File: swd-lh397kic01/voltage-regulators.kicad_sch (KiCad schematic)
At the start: 10 parts, among them U1 RS3236-2.5FY5, U3 AP3127B

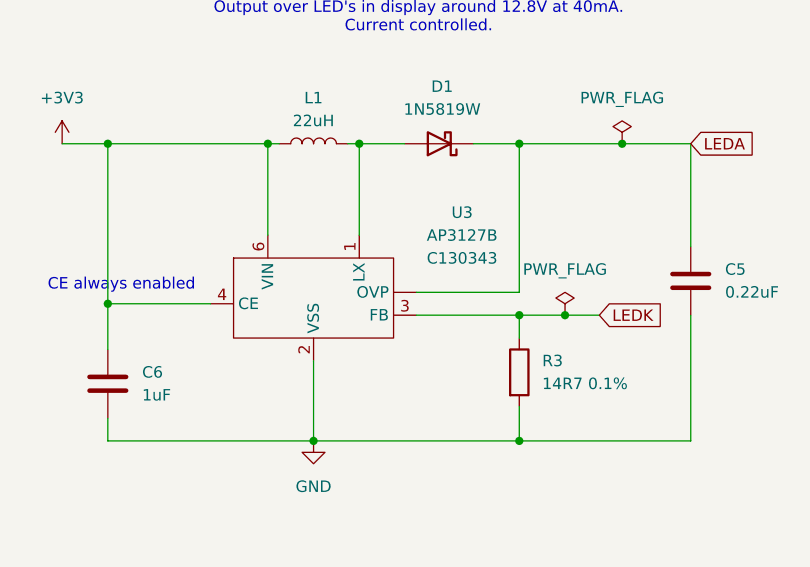
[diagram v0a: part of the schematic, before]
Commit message: Fix names, footprints, and silkscreen of the pcb's
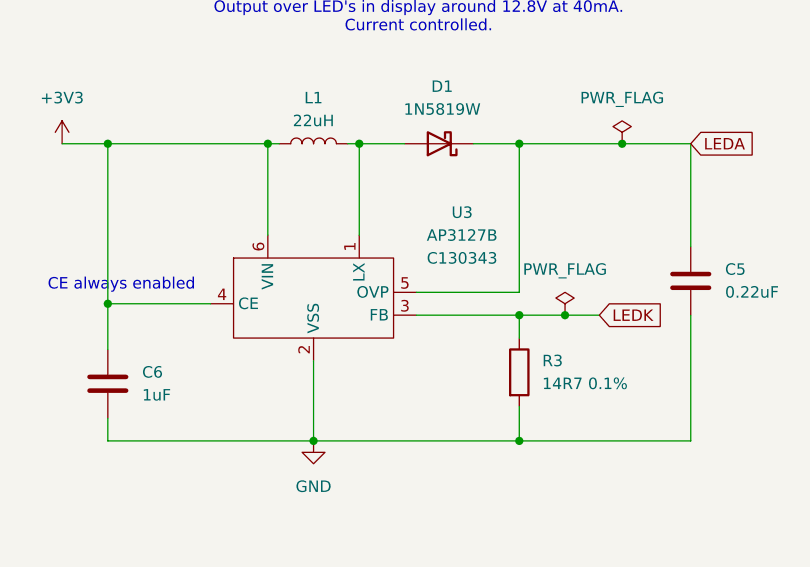
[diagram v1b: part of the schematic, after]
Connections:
- net LEDA: now also U3.5 (OVP); no longer U3. (OVP)
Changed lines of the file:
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@@
 		(pin "1"
 		)
-		(pin ""
+		(pin "5"
 		)
 		(pin "2"

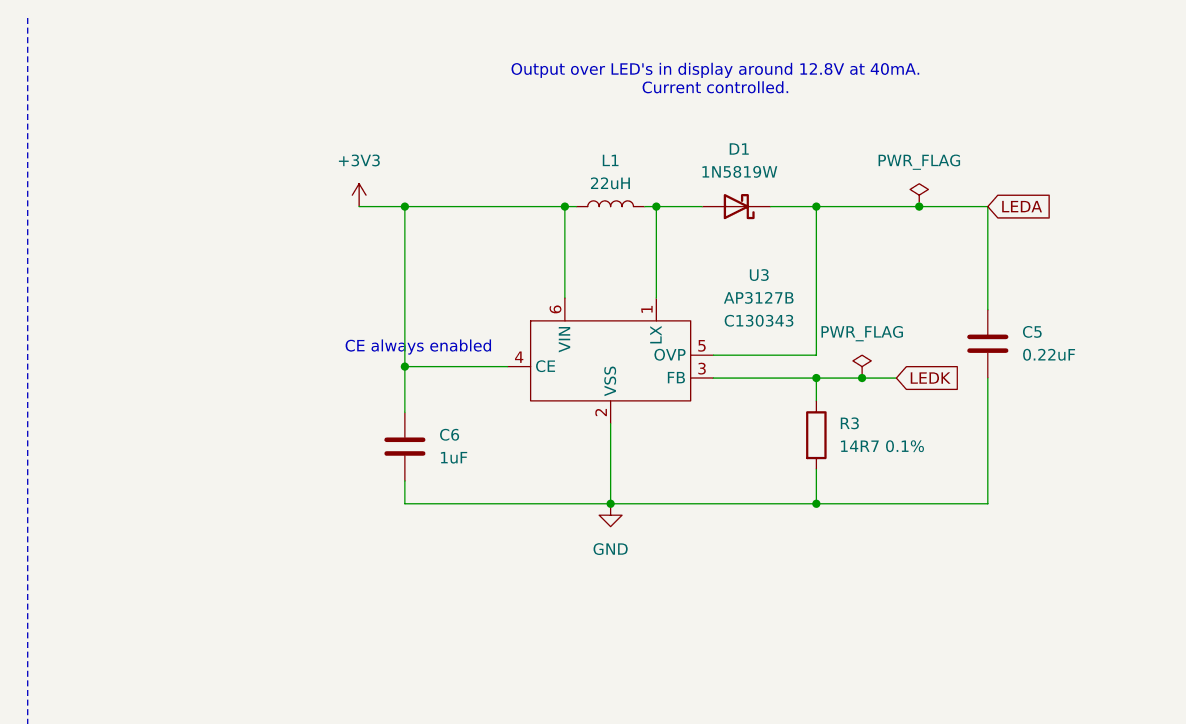
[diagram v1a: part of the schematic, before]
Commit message: Add LCSC labels that were missing for swd lh397kic01
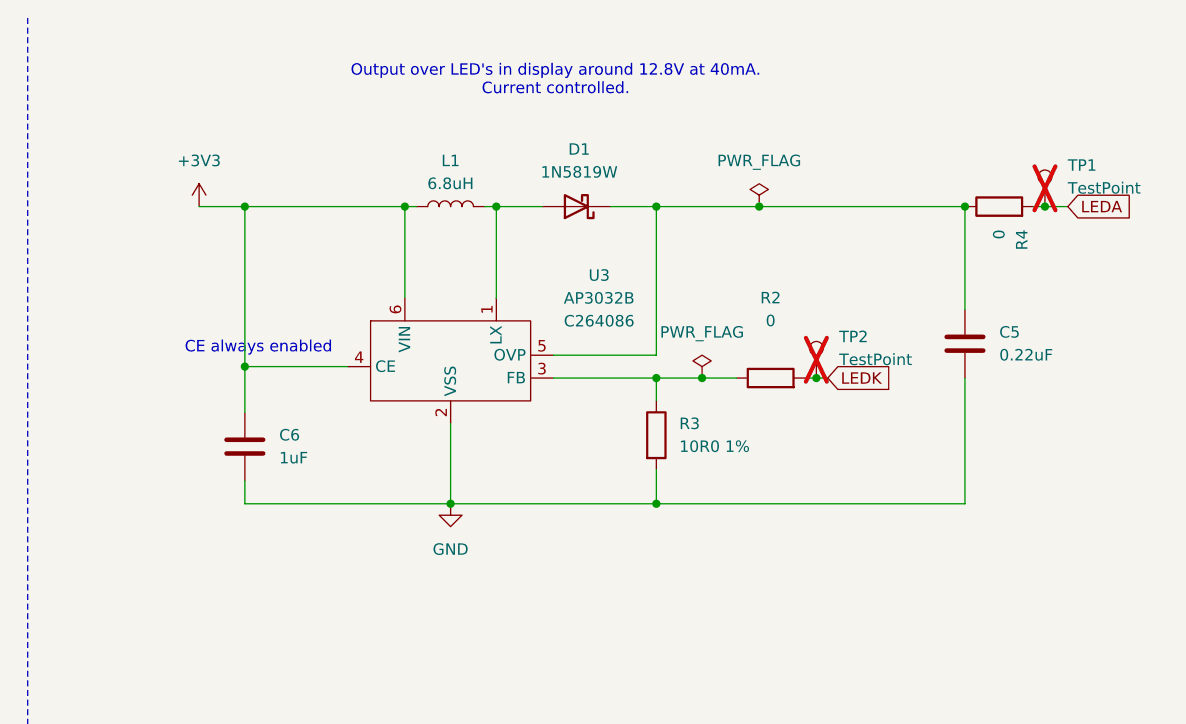
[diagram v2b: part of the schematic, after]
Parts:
- added R2, R4: 0, Resistor_SMD:R_0603_1608Metric, symbol Device:R
- added TP1, TP2: TestPoint, TestPoint:TestPoint_Pad_D1.0mm, symbol Connector:TestPoint
- C1, C2, C3, C6: LCSC C5189821 -> C386149
- L1: value 22uH -> 6.8uH; footprint Inductor_SMD:L_Changjiang_FNR252010S -> Inductor_SMD:L_1210_3225Metric_Pad1.42x2.65mm_HandSolder; LCSC C486445 -> C394999
- R3: value 14R7 0.1% -> 10R0 1%; LCSC C861135 -> C103222
- U1: LCSC (none) -> C379345; Lcsc C379345 -> (none)
- U3: value AP3127B -> AP3032B; LCSC C130343 -> C264086
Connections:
- net LEDA: now also R4.2, TP1.1; no longer C5.1, D1.1 (K), U3.5 (OVP)
- net LEDK: now also R2.2, TP2.1; no longer R3.1, U3.3 (FB)
- new net: C5.1, D1.1 (K), R4.1, U3.5 (OVP)
- new net: R2.1, R3.1, U3.3 (FB)
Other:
- moved on the sheet: C5, C6, D1, L1, R3, U3
